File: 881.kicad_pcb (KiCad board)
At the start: 4 copper layers, 38 x 105 mm, 114 parts, among them J1 RUN/STOP, J10 RS IN, J11 CP IN, J12 MA IN, J13 CB IN, J14 CY IN, J15 OH IN, J16 CH IN, J2 SYNC24 CLK, J3 ASSIGN 1, J4 ASSIGN 2, J5 BD IN, J6 SD IN, J7 LT IN, J8 MT IN, J9 HT IN, P1 CONN_02X03, Q1 MMBT3904, Q10 MMBT3904, Q11 MMBT3904, Q12 MMBT3904, Q13 MMBT3904, Q14 MMBT3906, Q2 MMBT3904, Q3 MMBT3904, Q4 MMBT3904, Q5 MMBT3904, Q6 MMBT3904, Q7 MMBT3904, Q8 MMBT3904, Q9 MMBT3904, U1 74HC165, U2 74HC165, U7 74AHCT1G125GW, X1 MIDI OUT, X2 SYNC24

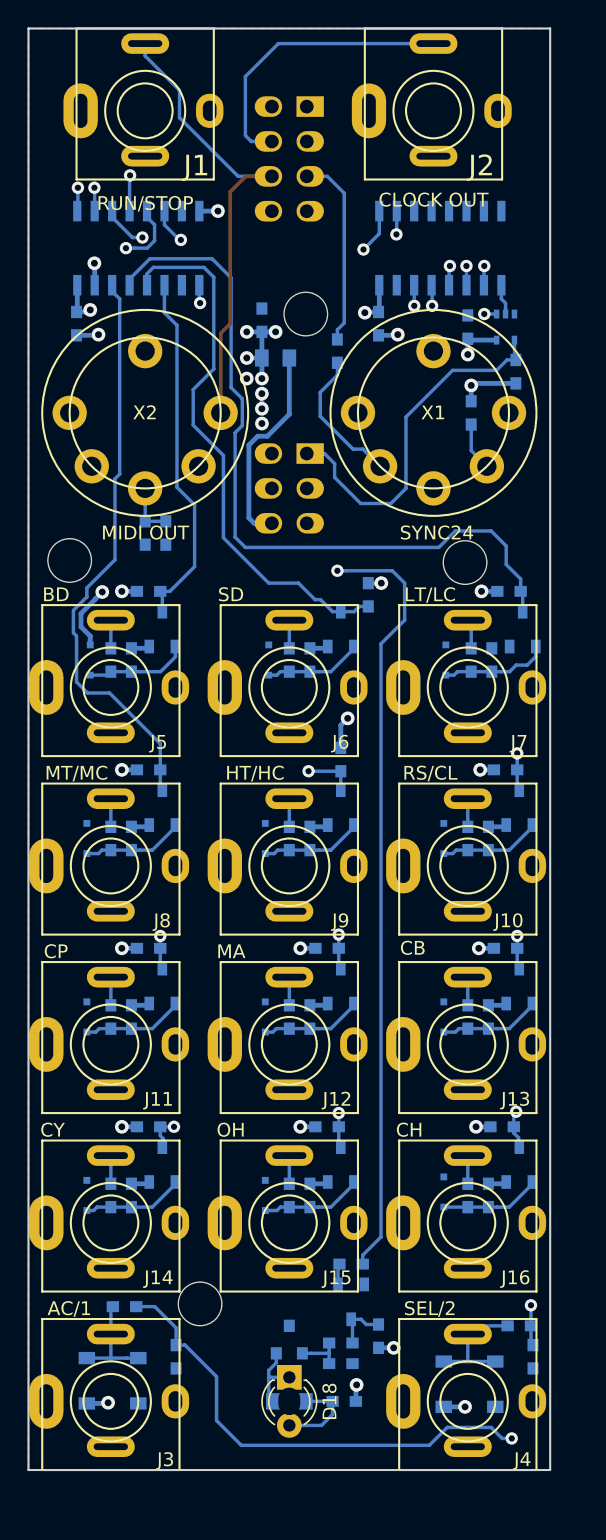
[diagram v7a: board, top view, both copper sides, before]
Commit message: DIN connector had wrong footprint. fixed. need to generate gerbers again before ordering
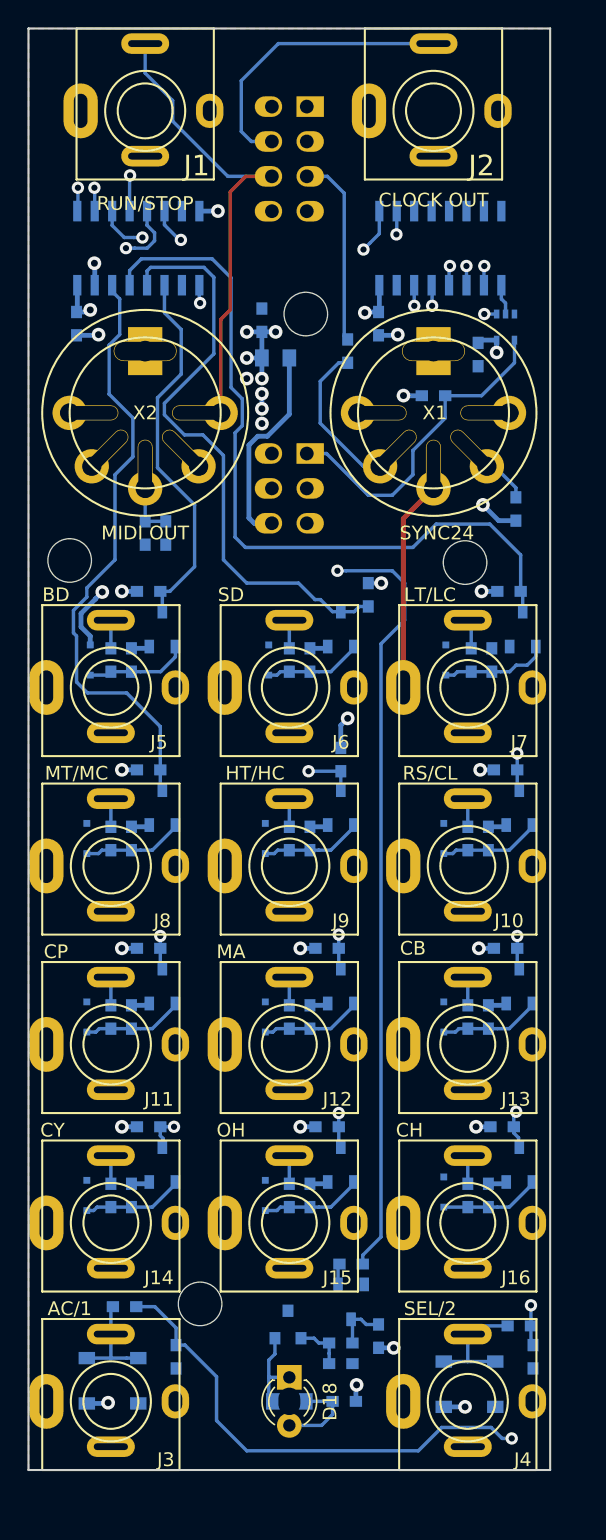
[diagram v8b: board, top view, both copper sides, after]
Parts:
- X1, X2: footprint MyModules:SD-50BV-5DIN -> MyModules:SD-50BV-5DIN-SLOTS
- moved R3 7.72 mm to (147.0, 90.0), turned to 270 degrees
- moved R44 6.25 mm to (141.0, 81.8), turned to 0 degrees
- moved C20 2.14 mm to (144.2, 78.8), turned to 270 degrees
- moved Q14 1.10 mm to (130.4, 149.4)
- moved R1 0.75 mm to (134.8, 78.5)
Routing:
- net GNDD: track 40.8 -> 55.1 mm
- net /SD: track 39.6 -> 43.2 mm
- net /CY: track 79.2 -> 82.0 mm
- net /MT: track 42.0 -> 44.2 mm
- net ISP_MISO: track 26.2 -> 24.0 mm
- net /MA: track 61.2 -> 63.1 mm
- net /HT: track 52.0 -> 53.8 mm
- net (no net): track 0.00 -> 1.61 mm
- net /CP: track 58.6 -> 60.1 mm
- net /BD: track 26.2 -> 27.6 mm
- net Net-(R3-Pad1): track 3.51 -> 2.25 mm
- net +5V: track 44.9 -> 43.7 mm, vias 28 -> 29
- net /OH: track 67.1 -> 68.2 mm
- net /CH: track 72.5 -> 73.5 mm
- net Net-(D17-Pad1): track 5.38 -> 6.44 mm
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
